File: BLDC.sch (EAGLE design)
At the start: 131 parts, among them J1 JST-1X7-MICRO, J2 JST-1X7-MICRO, J3 1-770174-1, J4 IPBT-102-H1-XX-S-RA, J5 IPBT-103-H1-XX-S-RA, J6 JST-1X7-MICRO, J7 JST-1X7-MICRO, J8 JST-1X7-MICRO, J9 JST-1X4-MICRO, Q1 IRFS7530TRLPBF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

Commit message: added stm32 LEDs
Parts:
- removed J3: 1-770174-1, FormE:1-770174-1
- removed R54, R55: 1k, adafruit:R-US_R0805
- added LED4: GREEN, FormE:LEDCHIP-LED0805
- added LED5: RED, FormE:5988110107F
- added R56, R57: 1k, adafruit:R-US_R0805
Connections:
- net LED_RED renamed LED_RED_1
- removed net AUX_10: R55.2, U2.PB5
- removed net AUX_9: R54.2, U2.PB4
- removed net LED_GREEN: LED1.A, U2.PC4
- new net LED_GREEN_1: LED4.A, U2.PC4
- new net LED_GREEN_2: LED1.A, U2.PB5
- new net LED_RED_2: LED5.A, U2.PB4
- new net N$38: LED4.C, R56.2
- new net N$39: LED5.C, R57.2
- net DGND: now also J4.1
- net GND: now also R56.1, R57.1; no longer R54.1, R55.1
- net H1_VS: now also J5.1
- net H2_VS: now also J5.2
- net H3_VS: now also J5.3
- net VCC: now also J4.2
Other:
- note added: "STM32 LEDS"
- moved on the sheet: C2, C7, J4, J5, LED1, LED2, R14, R15, R4, U1

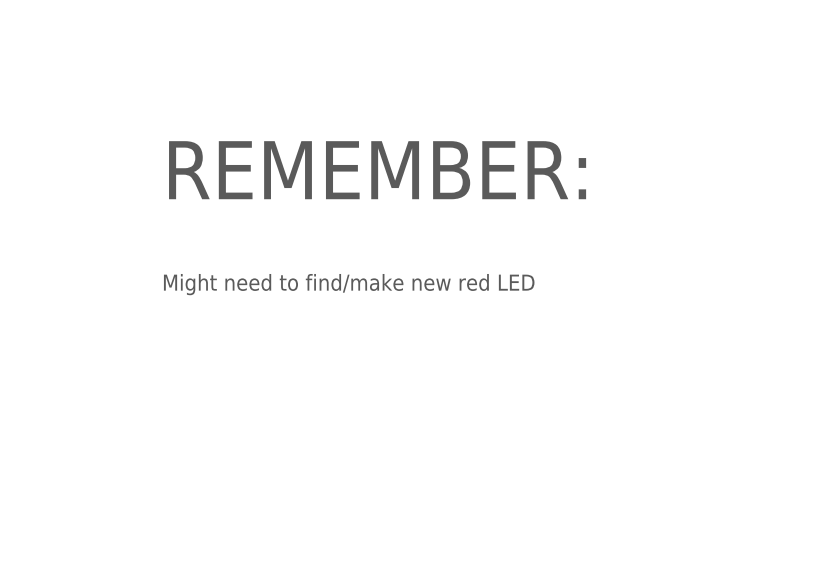
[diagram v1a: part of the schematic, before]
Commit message: only 8 aux now
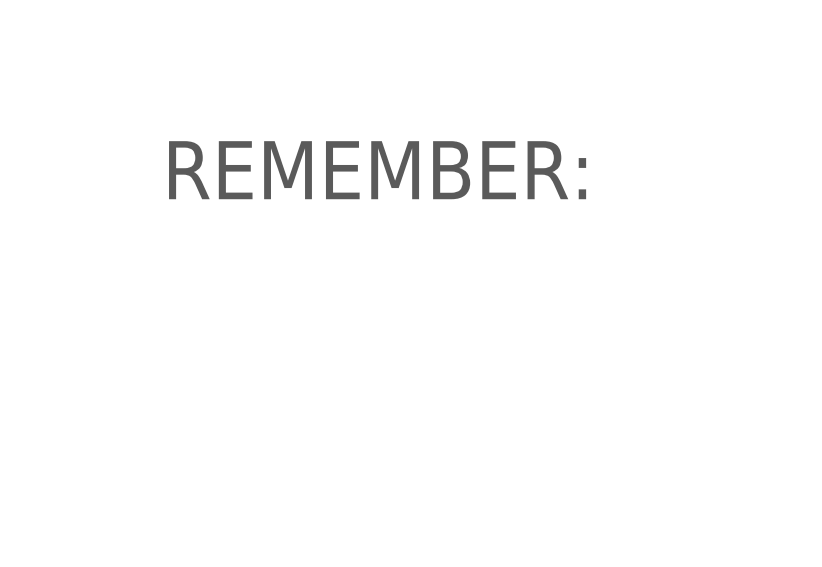
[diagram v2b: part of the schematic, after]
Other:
- note removed: "Might need to find/make new red LED"
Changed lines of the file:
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@@
 <wire x1="-137.16" y1="-129.54" x2="-137.16" y2="-71.12" width="0.6096" layer="95"/>
 <wire x1="-137.16" y1="-71.12" x2="-241.3" y2="-71.12" width="0.6096" layer="95"/>
-<text x="-256.54" y="160.02" size="1.778" layer="97">Might need to find/make new red LED</text>
 <text x="-256.54" y="170.18" size="6.4516" layer="97">REMEMBER:</text>
 <text x="-375.92" y="170.18" size="6.4516" layer="97">NEED?</text>

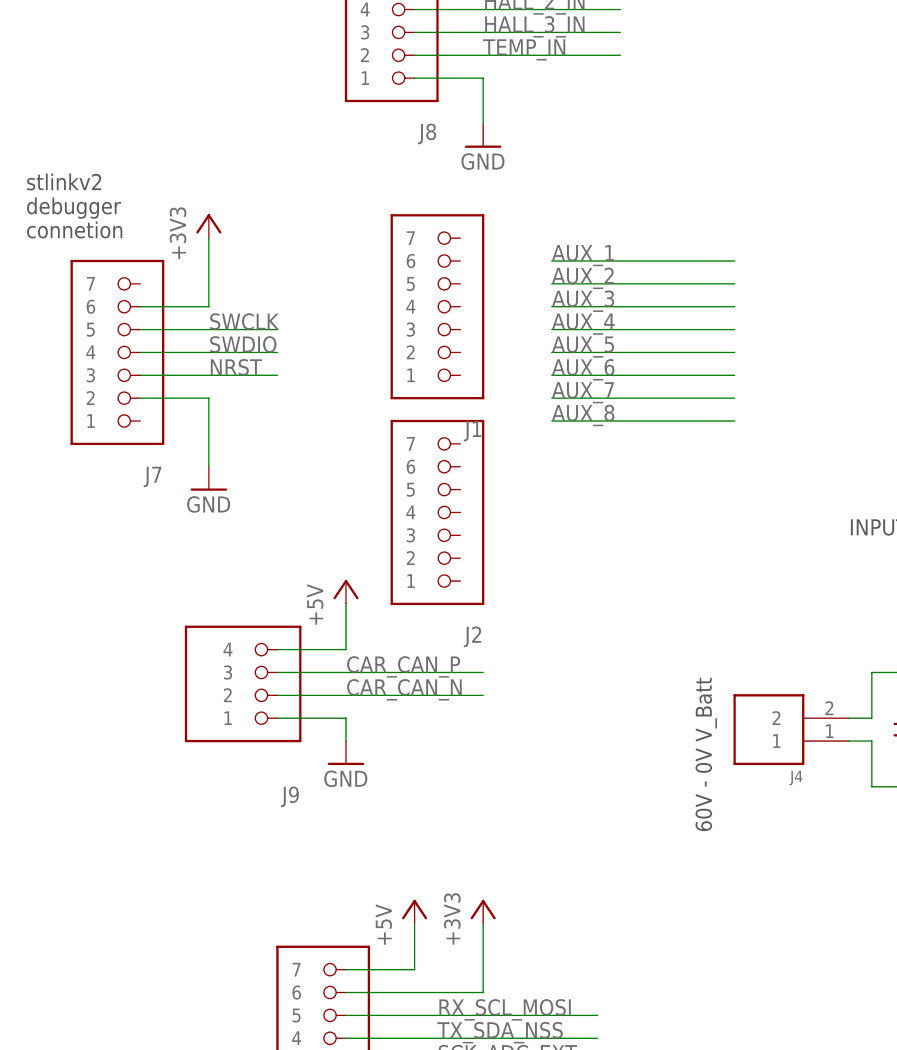
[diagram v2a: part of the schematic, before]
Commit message: commited to micro JST connectors
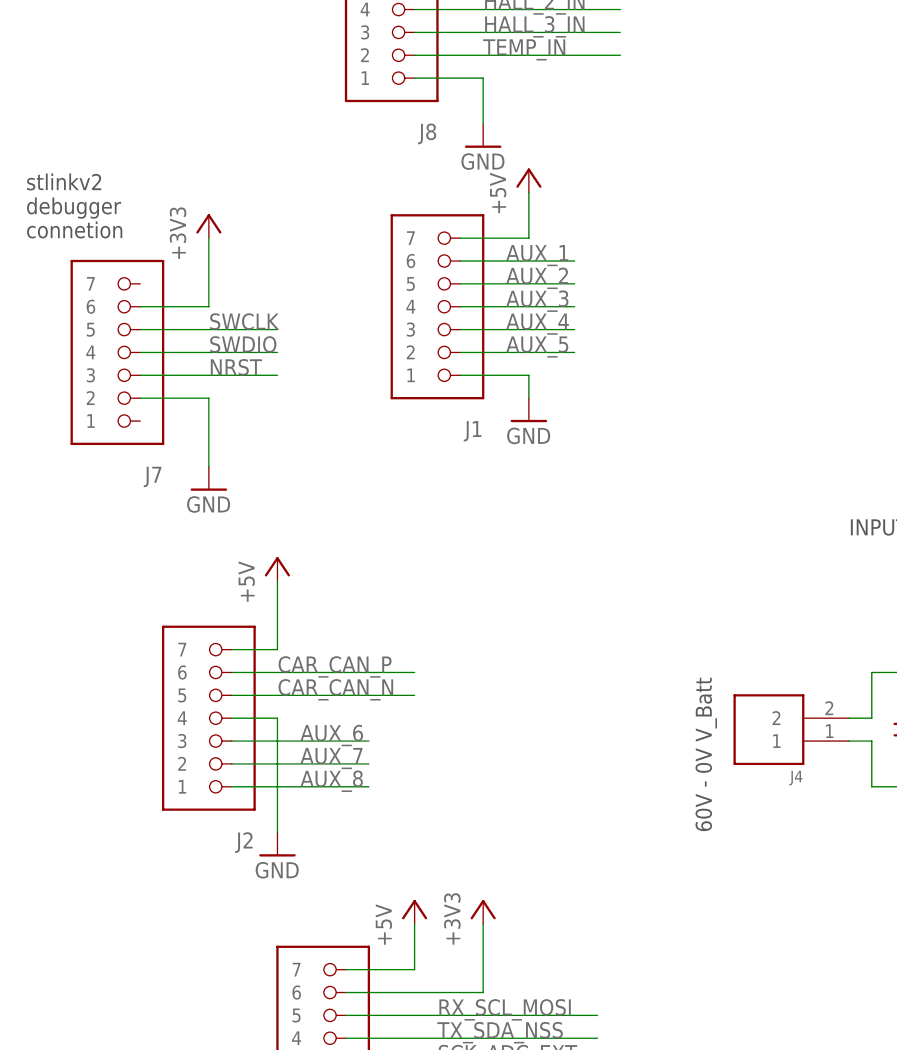
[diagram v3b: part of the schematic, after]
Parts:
- removed J9: JST-1X4-MICRO, FormE:JST-1X4-MICRO
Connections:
- net +5V: now also J1.7, J2.7; no longer J9.4
- net AUX_1: now also J1.6
- net AUX_2: now also J1.5
- net AUX_3: now also J1.4
- net AUX_4: now also J1.3
- net AUX_5: now also J1.2
- net AUX_6: now also J2.3
- net AUX_7: now also J2.2
- net AUX_8: now also J2.1
- net CAR_CAN_N: now also J2.5; no longer J9.2
- net CAR_CAN_P: now also J2.6; no longer J9.3
- net GND: now also J1.1, J2.4; no longer J9.1
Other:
- moved on the sheet: J2
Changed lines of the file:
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@@
 <part name="J7" library="FormE" deviceset="JST-1X7-MICRO" device="" value=""/>
 <part name="J8" library="FormE" deviceset="JST-1X7-MICRO" device="" value=""/>
-<part name="J9" library="FormE" deviceset="JST-1X4-MICRO" device="" value=""/>
 <part name="J1" library="FormE" deviceset="JST-1X7-MICRO" device="" value=""/>
 <part name="J2" library="FormE" deviceset="JST-1X7-MICRO" device="" value=""/>
@@
 <part name="GND46" library="supply1" deviceset="GND" device=""/>
 <part name="LED5" library="FormE" deviceset="5988110107F" device="" value="RED"/>
+<part name="P+15" library="supply1" deviceset="+5V" device=""/>
+<part name="GND47" library="supply1" deviceset="GND" device=""/>
 </parts>
 <sheets>
@@
 <instance part="GND3" gate="1" x="-269.24" y="-68.58"/>
 <instance part="P+2" gate="1" x="-269.24" y="-38.1"/>
-<instance part="P+1" gate="1" x="-276.86" y="-2.54"/>
-<instance part="GND2" gate="1" x="-276.86" y="-22.86"/>
+<instance part="P+1" gate="1" x="-284.48" y="0"/>
+<instance part="GND2" gate="1" x="-284.48" y="-33.02"/>
 <instance part="R8" gate="G$1" x="-157.48" y="-33.02" rot="R90">
 <attribute name="PARTNO" x="-157.48" y="-33.02" size="1.778" layer="96" display="off"/>
@@
 <instance part="J7" gate="G$1" x="-302.26" y="22.86" rot="R180"/>
 <instance part="J8" gate="G$1" x="-271.78" y="60.96" rot="R180"/>
-<instance part="J9" gate="G$1" x="-287.02" y="-12.7" rot="R180"/>
 <instance part="J1" gate="G$1" x="-266.7" y="27.94" rot="R180"/>
-<instance part="J2" gate="G$1" x="-266.7" y="5.08" rot="R180"/>
+<instance part="J2" gate="G$1" x="-292.1" y="-17.78" rot="R180"/>
 <instance part="J4" gate="G$1" x="-220.98" y="-20.32" rot="R180"/>
 <instance part="J5" gate="G$1" x="482.6" y="35.56"/>
@@
 <instance part="GND46" gate="1" x="-114.3" y="-121.92" rot="R270"/>
 <instance part="LED5" gate="G$1" x="-91.44" y="-121.92" rot="R270"/>
+<instance part="P+15" gate="1" x="-256.54" y="43.18"/>
+<instance part="GND47" gate="1" x="-256.54" y="15.24"/>
 </instances>
 <busses>
@@
 </segment>
 <segment>
-<wire x1="-284.48" y1="-17.78" x2="-276.86" y2="-17.78" width="0.1524" layer="91"/>
-<wire x1="-276.86" y1="-17.78" x2="-276.86" y2="-20.32" width="0.1524" layer="91"/>
+<wire x1="-289.56" y1="-17.78" x2="-284.48" y2="-17.78" width="0.1524" layer="91"/>
+<wire x1="-284.48" y1="-17.78" x2="-284.48" y2="-30.48" width="0.1524" layer="91"/>
 <pinref part="GND2" gate="1" pin="GND"/>
-<pinref part="J9" gate="G$1" pin="1"/>
+<pinref part="J2" gate="G$1" pin="4"/>
 </segment>
 <segment>
@@
 <wire x1="-111.76" y1="-121.92" x2="-109.22" y2="-121.92" width="0.1524" layer="91"/>
 </segment>
+<segment>
+<pinref part="GND47" gate="1" pin="GND"/>
+<wire x1="-256.54" y1="17.78" x2="-256.54" y2="20.32" width="0.1524" layer="91"/>
+<pinref part="J1" gate="G$1" pin="1"/>
+<wire x1="-256.54" y1="20.32" x2="-264.16" y2="20.32" width="0.1524" layer="91"/>
+</segment>
 </net>
 <net name="+5V" class="0">
@@
 </segment>
 <segment>
-<wire x1="-284.48" y1="-10.16" x2="-276.86" y2="-10.16" width="0.1524" layer="91"/>
-<wire x1="-276.86" y1="-10.16" x2="-276.86" y2="-5.08" width="0.1524" layer="91"/>
+<wire x1="-289.56" y1="-10.16" x2="-284.48" y2="-10.16" width="0.1524" layer="91"/>
+<wire x1="-284.48" y1="-10.16" x2="-284.48" y2="-2.54" width="0.1524" layer="91"/>
 <pinref part="P+1" gate="1" pin="+5V"/>
-<pinref part="J9" gate="G$1" pin="4"/>
+<pinref part="J2" gate="G$1" pin="7"/>
 </segment>
 <segment>
@@
 <pinref part="P+8" gate="1" pin="+5V"/>
 <wire x1="132.08" y1="91.44" x2="132.08" y2="93.98" width="0.1524" layer="91"/>
+</segment>
+<segment>
+<pinref part="J1" gate="G$1" pin="7"/>
+<pinref part="P+15" gate="1" pin="+5V"/>
+<wire x1="-264.16" y1="35.56" x2="-256.54" y2="35.56" width="0.1524" layer="91"/>
+<wire x1="-256.54" y1="35.56" x2="-256.54" y2="40.64" width="0.1524" layer="91"/>
 </segment>
 </net>
@@
 </segment>
 <segment>
-<wire x1="-284.48" y1="-12.7" x2="-261.62" y2="-12.7" width="0.1524" layer="91"/>
-<label x="-276.86" y="-12.7" size="1.778" layer="95"/>
-<pinref part="J9" gate="G$1" pin="3"/>
+<wire x1="-289.56" y1="-12.7" x2="-269.24" y2="-12.7" width="0.1524" layer="91"/>
+<label x="-284.48" y="-12.7" size="1.778" layer="95"/>
+<pinref part="J2" gate="G$1" pin="6"/>
 </segment>
 </net>
@@
 </segment>
 <segment>
-<wire x1="-284.48" y1="-15.24" x2="-261.62" y2="-15.24" width="0.1524" layer="91"/>
-<label x="-276.86" y="-15.24" size="1.778" layer="95"/>
-<pinref part="J9" gate="G$1" pin="2"/>
+<wire x1="-289.56" y1="-15.24" x2="-269.24" y2="-15.24" width="0.1524" layer="91"/>
+<label x="-284.48" y="-15.24" size="1.778" layer="95"/>
+<pinref part="J2" gate="G$1" pin="5"/>
 </segment>
 </net>
@@
 <net name="AUX_1" class="0">
 <segment>
-<wire x1="-254" y1="33.02" x2="-233.68" y2="33.02" width="0.1524" layer="91"/>
-<label x="-254" y="33.02" size="1.778" layer="95"/>
+<wire x1="-264.16" y1="33.02" x2="-251.46" y2="33.02" width="0.1524" layer="91"/>
+<label x="-259.08" y="33.02" size="1.778" layer="95"/>
+<pinref part="J1" gate="G$1" pin="6"/>
 </segment>
 <segment>
@@
 <net name="AUX_2" class="0">
 <segment>
-<wire x1="-254" y1="30.48" x2="-233.68" y2="30.48" width="0.1524" layer="91"/>
-<label x="-254" y="30.48" size="1.778" layer="95"/>
+<wire x1="-264.16" y1="30.48" x2="-251.46" y2="30.48" width="0.1524" layer="91"/>
+<label x="-259.08" y="30.48" size="1.778" layer="95"/>
+<pinref part="J1" gate="G$1" pin="5"/>
 </segment>
 <segment>
@@
 <net name="AUX_3" class="0">
 <segment>
-<wire x1="-254" y1="27.94" x2="-233.68" y2="27.94" width="0.1524" layer="91"/>
-<label x="-254" y="27.94" size="1.778" layer="95"/>
+<wire x1="-264.16" y1="27.94" x2="-251.46" y2="27.94" width="0.1524" layer="91"/>
+<label x="-259.08" y="27.94" size="1.778" layer="95"/>
+<pinref part="J1" gate="G$1" pin="4"/>
 </segment>
 <segment>
@@
 <net name="AUX_4" class="0">
 <segment>
-<wire x1="-254" y1="25.4" x2="-233.68" y2="25.4" width="0.1524" layer="91"/>
-<label x="-254" y="25.4" size="1.778" layer="95"/>
+<wire x1="-264.16" y1="25.4" x2="-251.46" y2="25.4" width="0.1524" layer="91"/>
+<label x="-259.08" y="25.4" size="1.778" layer="95"/>
+<pinref part="J1" gate="G$1" pin="3"/>
 </segment>
 <segment>
@@
 <net name="AUX_5" class="0">
 <segment>
-<wire x1="-254" y1="22.86" x2="-233.68" y2="22.86" width="0.1524" layer="91"/>
-<label x="-254" y="22.86" size="1.778" layer="95"/>
+<wire x1="-264.16" y1="22.86" x2="-251.46" y2="22.86" width="0.1524" layer="91"/>
+<label x="-259.08" y="22.86" size="1.778" layer="95"/>
+<pinref part="J1" gate="G$1" pin="2"/>
 </segment>
 <segment>
@@
 <net name="AUX_6" class="0">
 <segment>
-<wire x1="-254" y1="20.32" x2="-233.68" y2="20.32" width="0.1524" layer="91"/>
-<label x="-254" y="20.32" size="1.778" layer="95"/>
+<wire x1="-289.56" y1="-20.32" x2="-274.32" y2="-20.32" width="0.1524" layer="91"/>
+<label x="-281.94" y="-20.32" size="1.778" layer="95"/>
+<pinref part="J2" gate="G$1" pin="3"/>
 </segment>
 <segment>
@@
 </segment>
 <segment>
-<wire x1="-254" y1="17.78" x2="-233.68" y2="17.78" width="0.1524" layer="91"/>
-<label x="-254" y="17.78" size="1.778" layer="95"/>
+<wire x1="-289.56" y1="-22.86" x2="-274.32" y2="-22.86" width="0.1524" layer="91"/>
+<label x="-281.94" y="-22.86" size="1.778" layer="95"/>
+<pinref part="J2" gate="G$1" pin="2"/>
 </segment>
 <segment>
@@
 </segment>
 <segment>
-<wire x1="-254" y1="15.24" x2="-233.68" y2="15.24" width="0.1524" layer="91"/>
-<label x="-254" y="15.24" size="1.778" layer="95"/>
-</segment>
-<segment>
+<wire x1="-289.56" y1="-25.4" x2="-274.32" y2="-25.4" width="0.1524" layer="91"/>
+<label x="-281.94" y="-25.4" size="1.778" layer="95"/>
+<pinref part="J2" gate="G$1" pin="1"/>
+</segment>
+<segment>

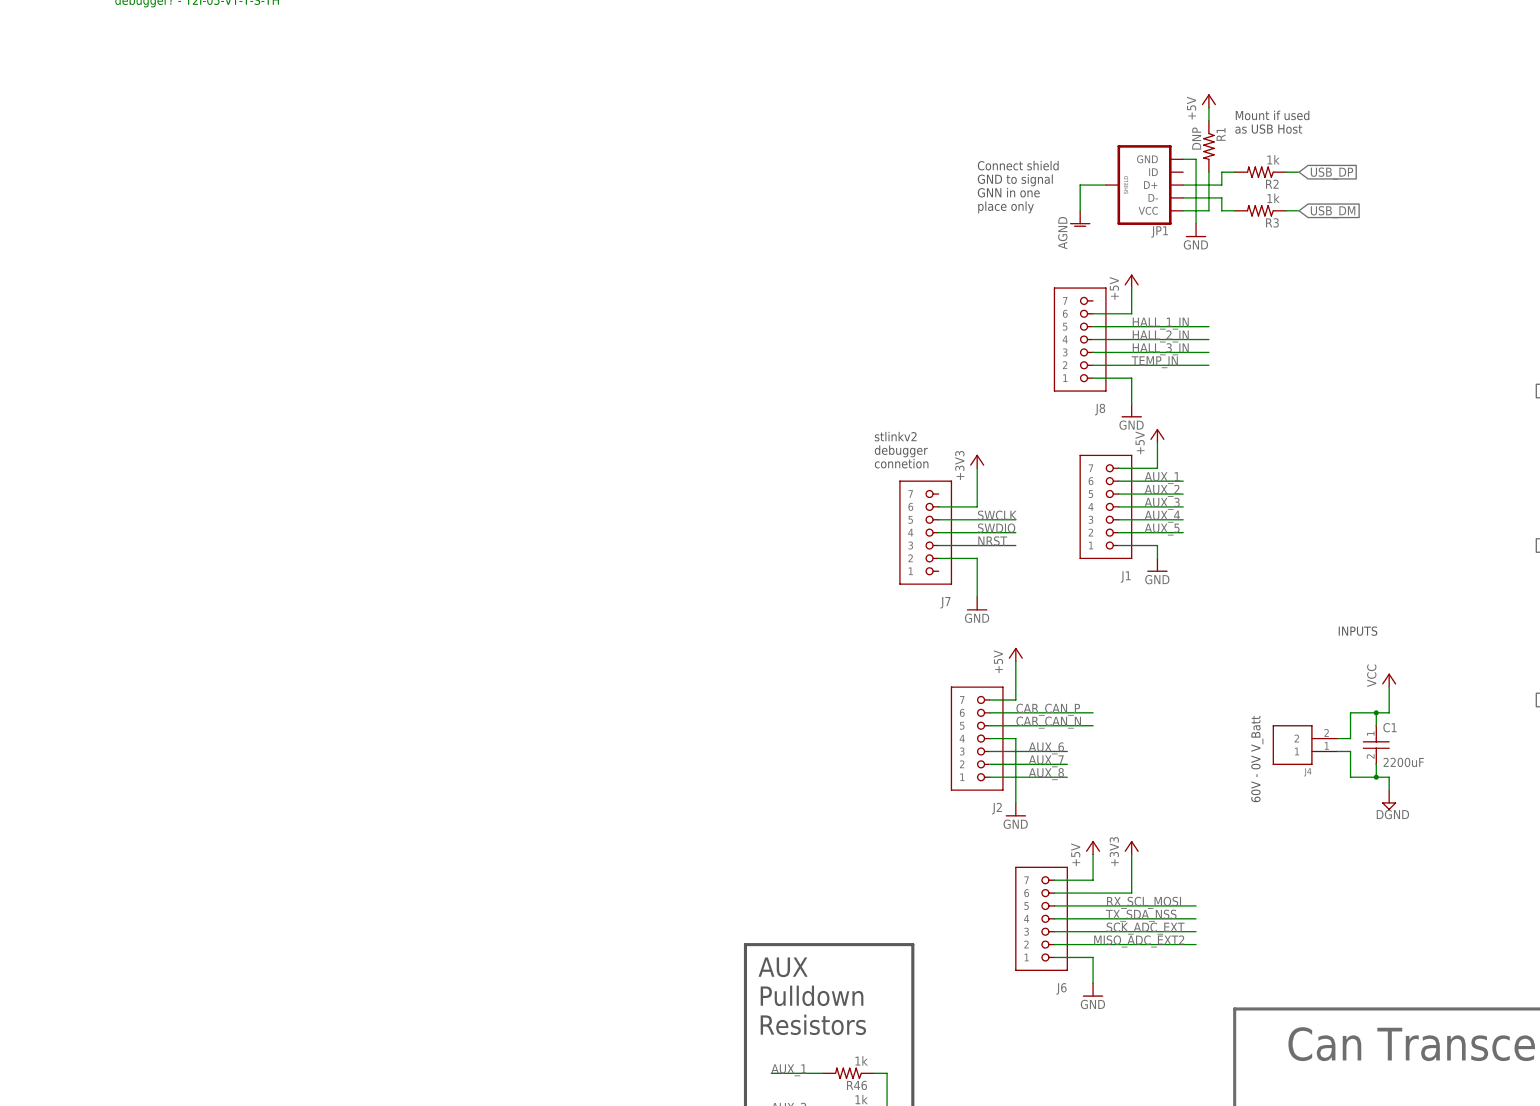
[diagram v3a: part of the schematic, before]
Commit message: made very rough boarder dimentions and hole placement
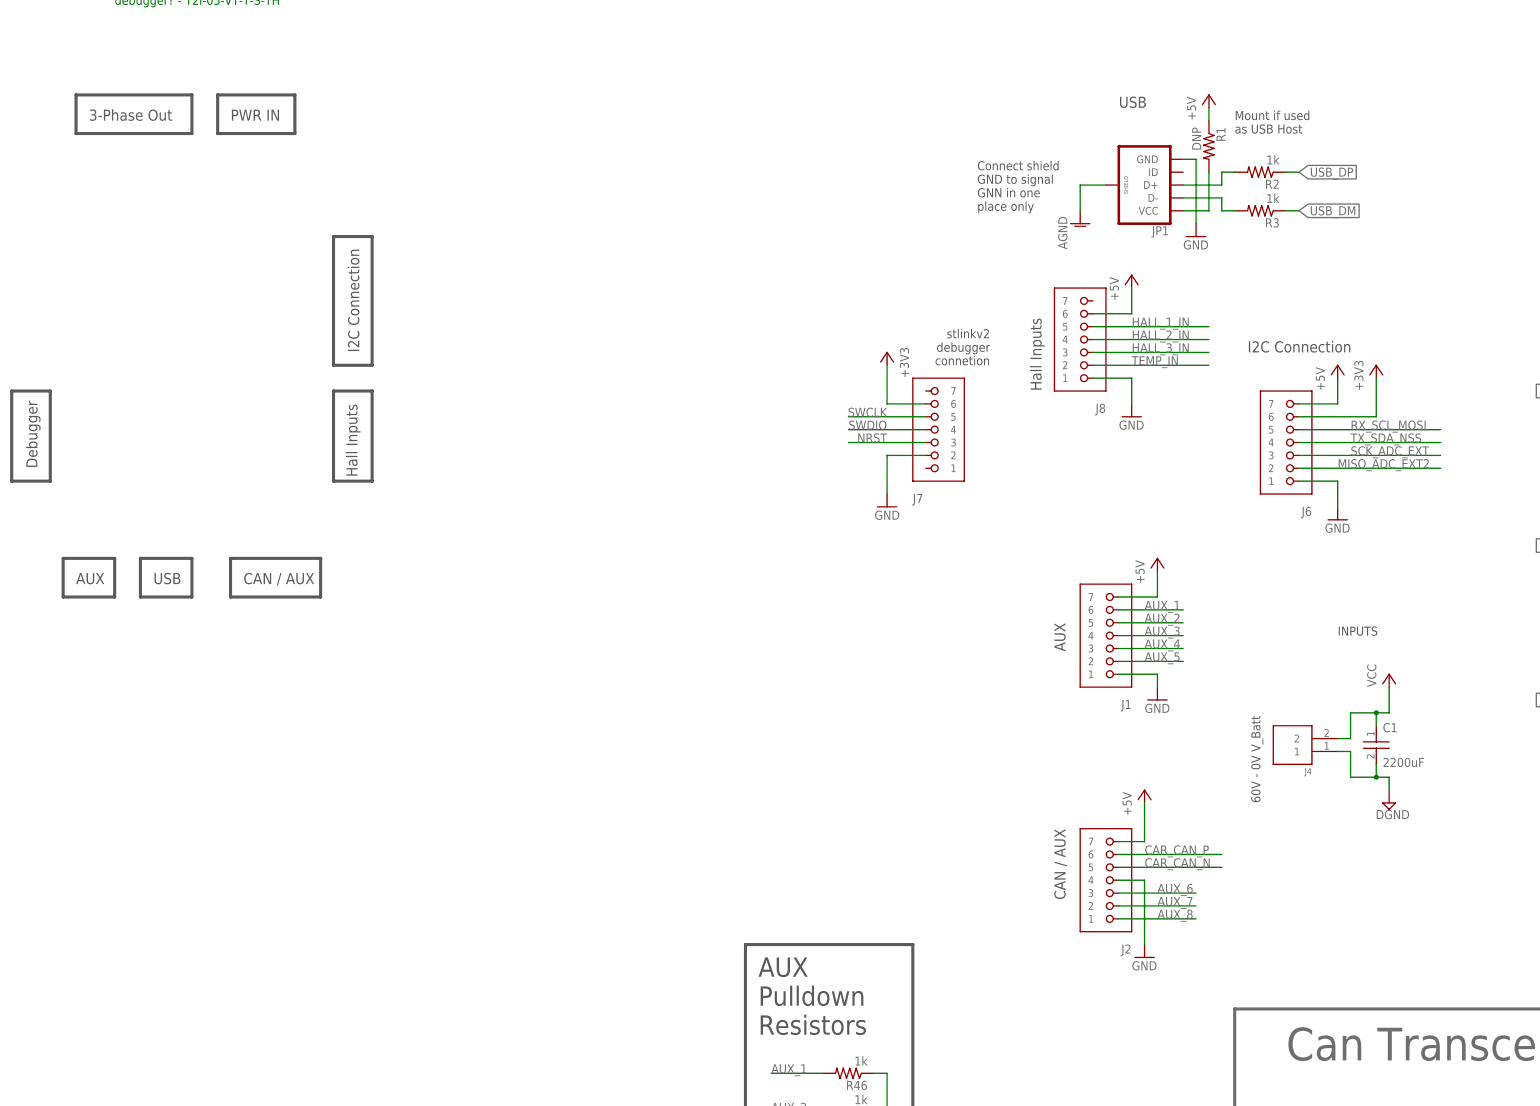
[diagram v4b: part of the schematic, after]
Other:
- note added: "3-Phase Out"
- note added: "AUX"
- note added: "CAN / AUX"
- note added: "Debugger"
- note added: "Hall Inputs"
- note added: "I2C Connection"
- note added: "PWR IN"
- note added: "USB"
- moved on the sheet: J1, J2, J6, J7
